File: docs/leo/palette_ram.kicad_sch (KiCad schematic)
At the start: 15 parts, among them IC10 74LS273, IC15 MB81C78A, IC16 MB81C78A, IC17 74153, IC18 74153, IC19 74153, IC22 74LS245, IC23 74LS245, IC25 74153, IC26 74153, IC27 74153, IC28 74153, IC30 74LS374, IC31 74LS374, IC9 74LS273

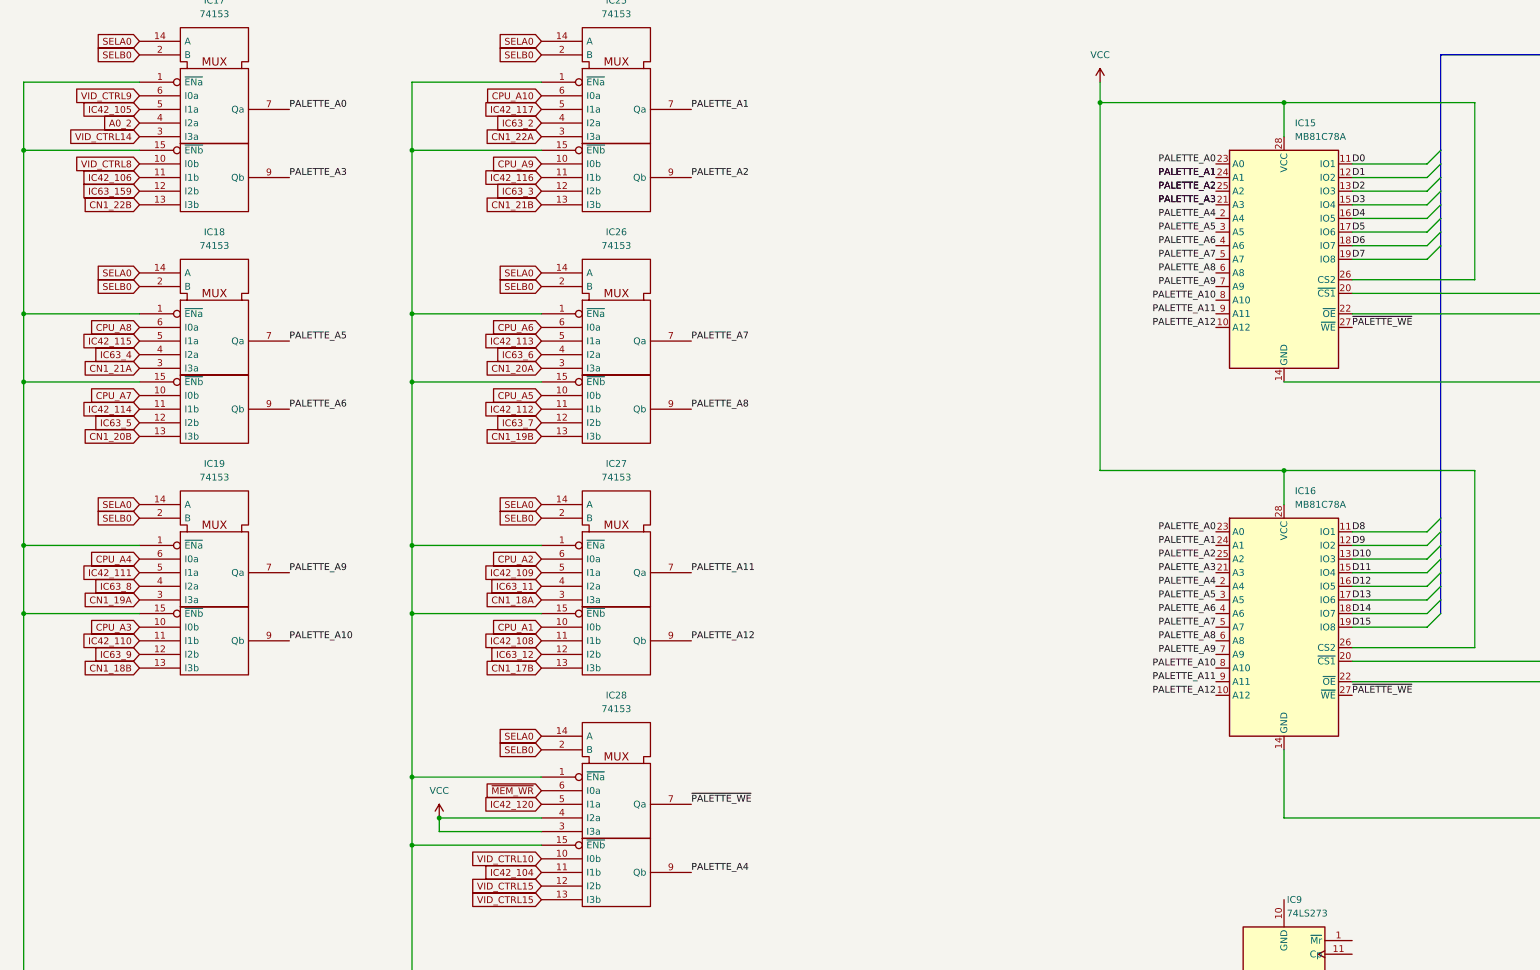
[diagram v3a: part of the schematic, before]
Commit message: Name video control bits Correct palette addressing
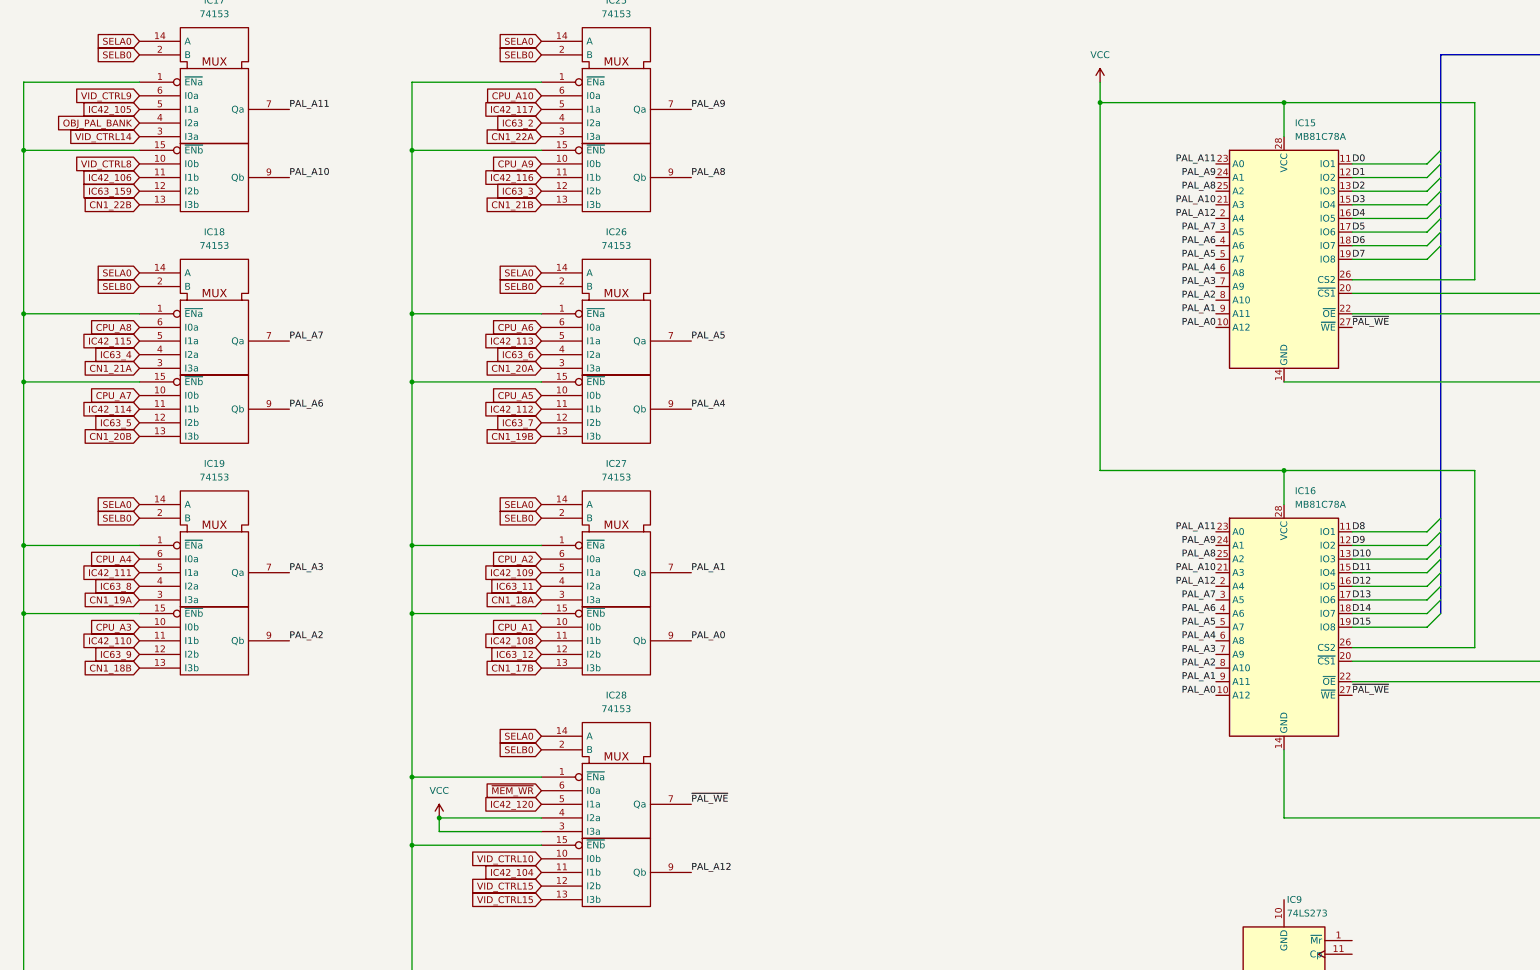
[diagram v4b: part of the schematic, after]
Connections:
- net A0_2 renamed OBJ_PAL_BANK
- net PALETTE_A0 renamed PAL_A11
- net PALETTE_A1 renamed PAL_A9
- net PALETTE_A10 renamed PAL_A2
- net PALETTE_A11 renamed PAL_A1
- net PALETTE_A12 renamed PAL_A0
- net PALETTE_A2 renamed PAL_A8
- net PALETTE_A3 renamed PAL_A10
- net PALETTE_A4 renamed PAL_A12
- net PALETTE_A5 renamed PAL_A7
- net PALETTE_A6 renamed PAL_A6
- net PALETTE_A7 renamed PAL_A5
- net PALETTE_A8 renamed PAL_A4
- net PALETTE_A9 renamed PAL_A3
- net ~{PALETTE_WE} renamed ~{PAL_WE}
